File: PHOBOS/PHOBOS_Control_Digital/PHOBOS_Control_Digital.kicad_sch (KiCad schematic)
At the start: 71 parts, among them IC1 MAPS-010144-TR0500, J1 Conn_01x06, J10 PS4, J11 PWR, J2 RF_OUT, J3 USB4056-03-A_REVA2, J4 Screw_Terminal_01x02, J5 Conn_02x15_Odd_Even, J6 PS1, J7 PS2, J8 Conn_01x02, J9 PS3, SW1 KMR211GLFS, U1 SX1280IMLTRT, U2 W25Q128JVSIQ, U3 NCP1117-3.3_SOT223, U4 RP2040, Y1 C1E-52.000-10-1012-X-M, Y2 ABM8-272-T3

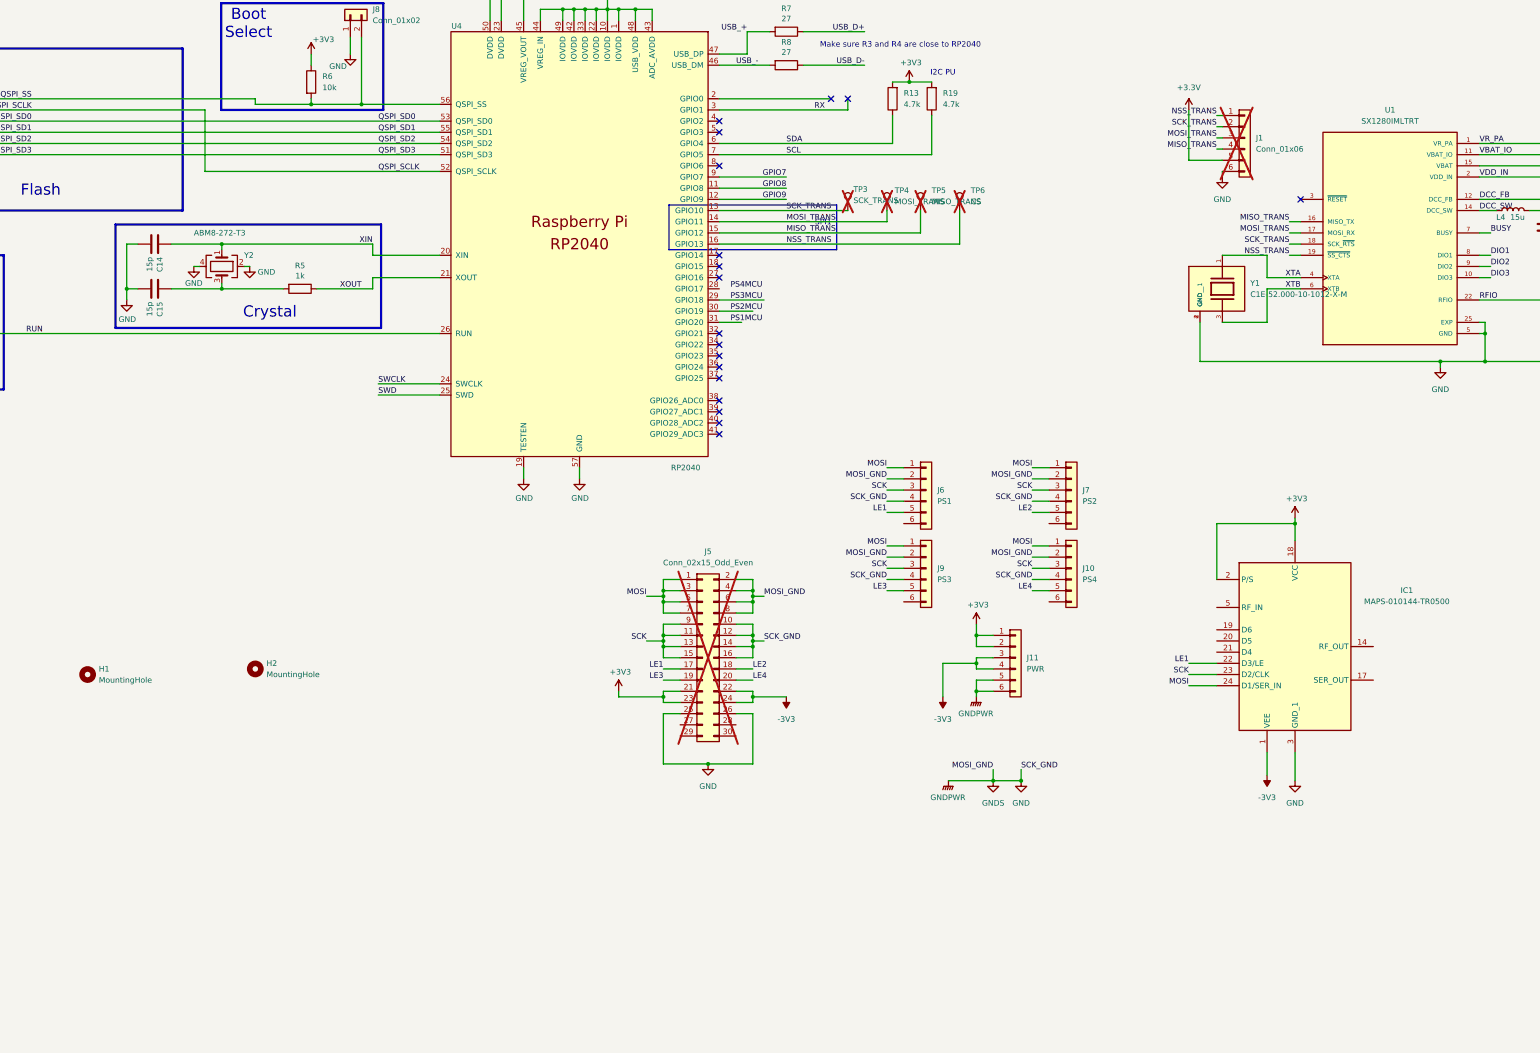
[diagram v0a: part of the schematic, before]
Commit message: connectors fine tuned (JST-GH 10 pin). 3v Inverter added. Needs routing
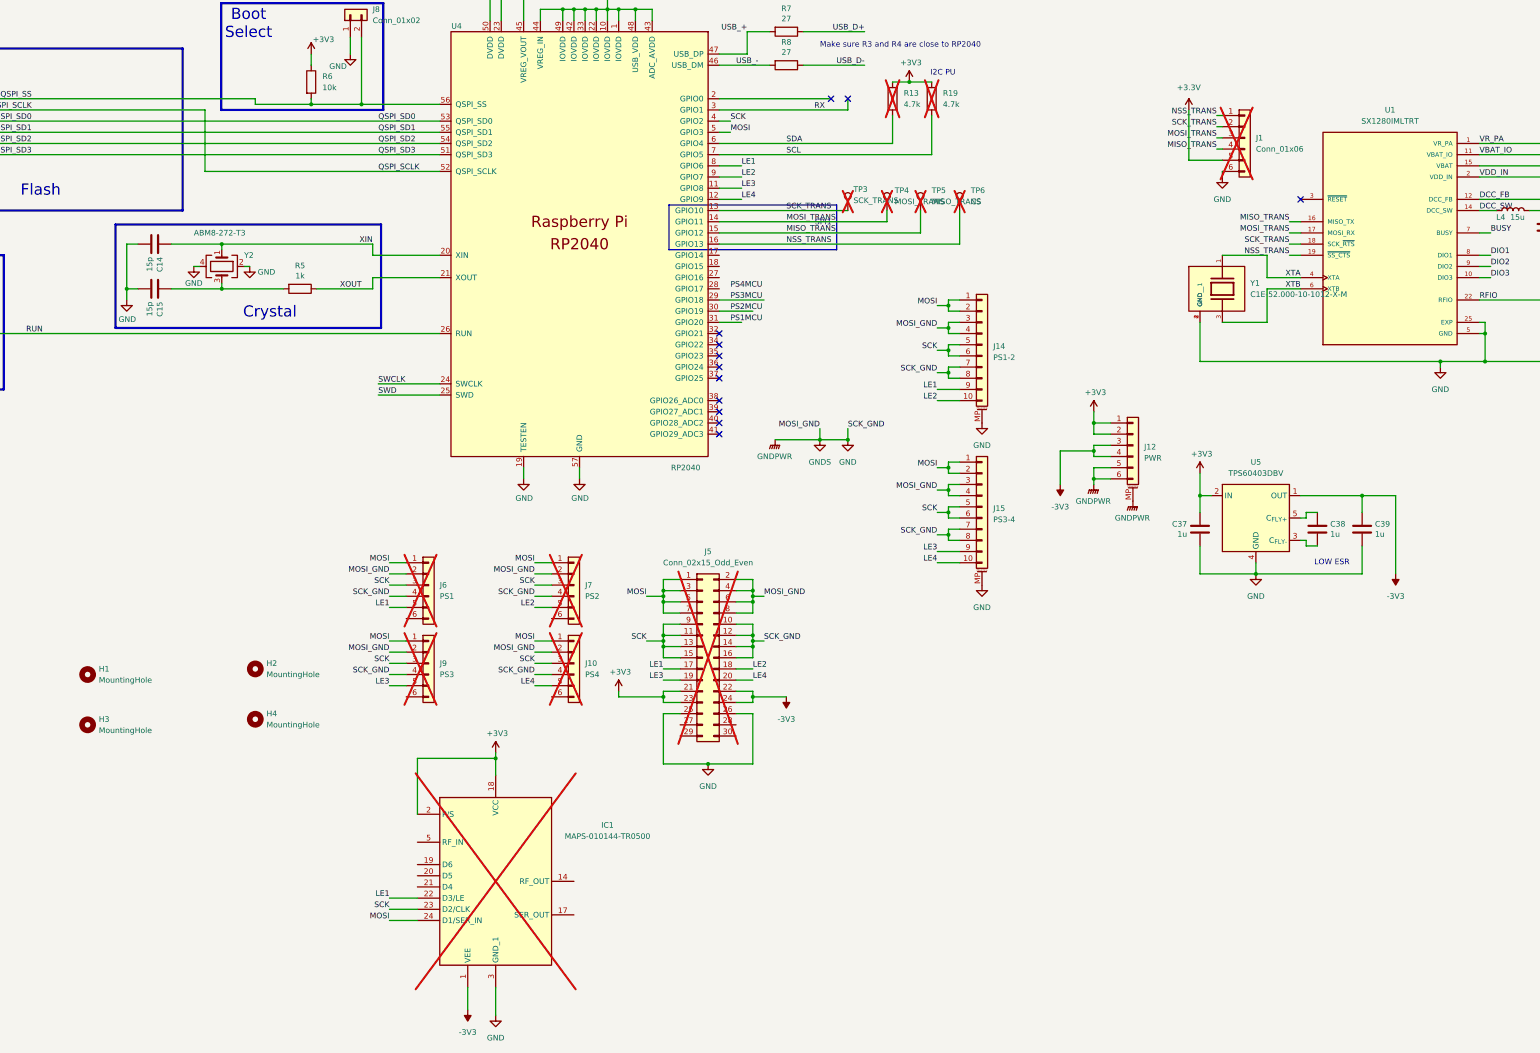
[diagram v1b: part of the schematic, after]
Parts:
- removed J11: PWR, Connector_JST:JST_GH_SM05B-GHS-TB_1x05-1MP_P1.25mm_Horizontal, symbol Connector_Generic:Conn_01x06
- added C37, C38, C39: 1u, Capacitor_SMD:C_0402_1005Metric, symbol Device:C
- added H3, H4: MountingHole, MountingHole:MountingHole_3.2mm_M3, symbol Mechanical:MountingHole
- added J12: PWR, Connector_JST:JST_GH_SM06B-GHS-TB_1x06-1MP_P1.25mm_Horizontal, symbol Connector_Generic_MountingPin:Conn_01x06_MountingPin
- added J14: PS1-2, Connector_JST:JST_GH_SM10B-GHS-TB_1x10-1MP_P1.25mm_Horizontal, symbol Connector_Generic_MountingPin:Conn_01x10_MountingPin
- added J15: PS3-4, Connector_JST:JST_GH_SM10B-GHS-TB_1x10-1MP_P1.25mm_Horizontal, symbol Connector_Generic_MountingPin:Conn_01x10_MountingPin
- added U5: TPS60403DBV, Package_TO_SOT_SMD:SOT-23-5, symbol Regulator_SwitchedCapacitor:TPS60403DBV
- IC1, J10, J6, J7, J9, R13, R19: now not fitted; now left out of the parts list
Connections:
- net GPIO7 is gone; now on net LE2: U4.9 (GPIO7)
- net GPIO8 is gone; now on net LE3: U4.11 (GPIO8)
- net GPIO9 is gone; now on net LE4: U4.12 (GPIO9)
- net +3V3: now also C37.1, J12.1 (Pin_1), J12.2 (Pin_2), U5.2 (IN)
- net -3V3: now also C39.1, J12.3 (Pin_3), J12.4 (Pin_4), U5.1 (OUT)
- net GND: now also C37.2, C39.2, J12.5 (Pin_5), J12.6 (Pin_6), J12.MP (MountPin), J14.3 (Pin_3), J14.4 (Pin_4), J14.7 (Pin_7), J14.8 (Pin_8), J14.MP (MountPin), J15.3 (Pin_3), J15.4 (Pin_4), J15.7 (Pin_7), J15.8 (Pin_8), J15.MP (MountPin), U5.4 (GND)
- net LE1: now also U4.8 (GPIO6), J14.9 (Pin_9)
- net LE2: now also J14.10 (Pin_10)
- net LE3: now also J15.9 (Pin_9)
- net LE4: now also J15.10 (Pin_10)
- net MOSI: now also U4.5 (GPIO3), J14.1 (Pin_1), J14.2 (Pin_2), J15.1 (Pin_1), J15.2 (Pin_2)
- net SCK: now also U4.4 (GPIO2), J14.5 (Pin_5), J14.6 (Pin_6), J15.5 (Pin_5), J15.6 (Pin_6)
- new net: C38.2, U5.3 (C_{FLY-})
- new net: C38.1, U5.5 (C_{FLY+})
- no-connect marks 28 -> 22
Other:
- note added: "LOW ESR"

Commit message: Centered and nicer layout.
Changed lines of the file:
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@@
 		(fields_autoplaced yes)
 		(property "Reference" "IC1"
-			(at 293.37 354.2598 0)
+			(at 270.1133 342.9 0)
 			(show_name no)
 			(do_not_autoplace no)
@@
 					(size 1.27 1.27)
 				)
+				(justify left)
 			)
 		)
 		(property "Value" "MAPS-010144-TR0500"
-			(at 293.37 356.7998 0)
+			(at 270.1133 345.44 0)
 			(show_name no)
 			(do_not_autoplace no)
@@
 					(size 1.27 1.27)
 				)
+				(justify left)
 			)
 		)

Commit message: Re-Centered. M3 bolt model added. SMA shifted to top side. Hole zones redone.
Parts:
- C37, C38, C39: footprint Capacitor_SMD:C_0402_1005Metric -> Capacitor_SMD:C_0603_1608Metric
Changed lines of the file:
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@@
 			(justify left bottom)
 		)
-		(property "Netclass" "PWR"
+		(property "Net Class" "PWR"
 			(at 183.5785 101.6 0)
 			(show_name no)
@@
 			(justify left bottom)
 		)
-		(property "Netclass" "PWR"
+		(property "Net Class" "PWR"
 			(at 165.7985 101.6 0)
 			(show_name no)
@@
 			)
 		)
-		(property "Footprint" "Capacitor_SMD:C_0402_1005Metric"
+		(property "Footprint" "Capacitor_SMD:C_0603_1608Metric"
 			(at 427.0248 290.83 0)
 			(hide yes)
@@
 			)
 		)
-		(property "Footprint" "Capacitor_SMD:C_0402_1005Metric"
+		(property "Footprint" "Capacitor_SMD:C_0603_1608Metric"
 			(at 465.7852 290.83 0)
 			(hide yes)
@@
 			)
 		)
-		(property "Footprint" "Capacitor_SMD:C_0402_1005Metric"
+		(property "Footprint" "Capacitor_SMD:C_0603_1608Metric"
 			(at 455.6252 290.83 0)
 			(hide yes)

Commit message: Images Added
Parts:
- removed IC1: MAPS-010144-TR0500, MAPS-010144-TR0500:QFN50P400X400X100-25N-D, symbol MAPS-010144-TR0500:MAPS-010144-TR0500
- removed J10: PS4, Connector_JST:JST_GH_SM05B-GHS-TB_1x05-1MP_P1.25mm_Horizontal, symbol Connector_Generic:Conn_01x06
- removed J5: Conn_02x15_Odd_Even, Package_CSP:Xilinx_CSG48_7.0x7.0mm_Layout7x7_P0.8mm, symbol Connector_Generic:Conn_02x15_Odd_Even
- removed J6: PS1, Connector_JST:JST_GH_SM05B-GHS-TB_1x05-1MP_P1.25mm_Horizontal, symbol Connector_Generic:Conn_01x06
- removed J7: PS2, Connector_JST:JST_GH_SM05B-GHS-TB_1x05-1MP_P1.25mm_Horizontal, symbol Connector_Generic:Conn_01x06
- removed J9: PS3, Connector_JST:JST_GH_SM05B-GHS-TB_1x05-1MP_P1.25mm_Horizontal, symbol Connector_Generic:Conn_01x06
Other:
- moved on the sheet: H1, H2, H3, H4

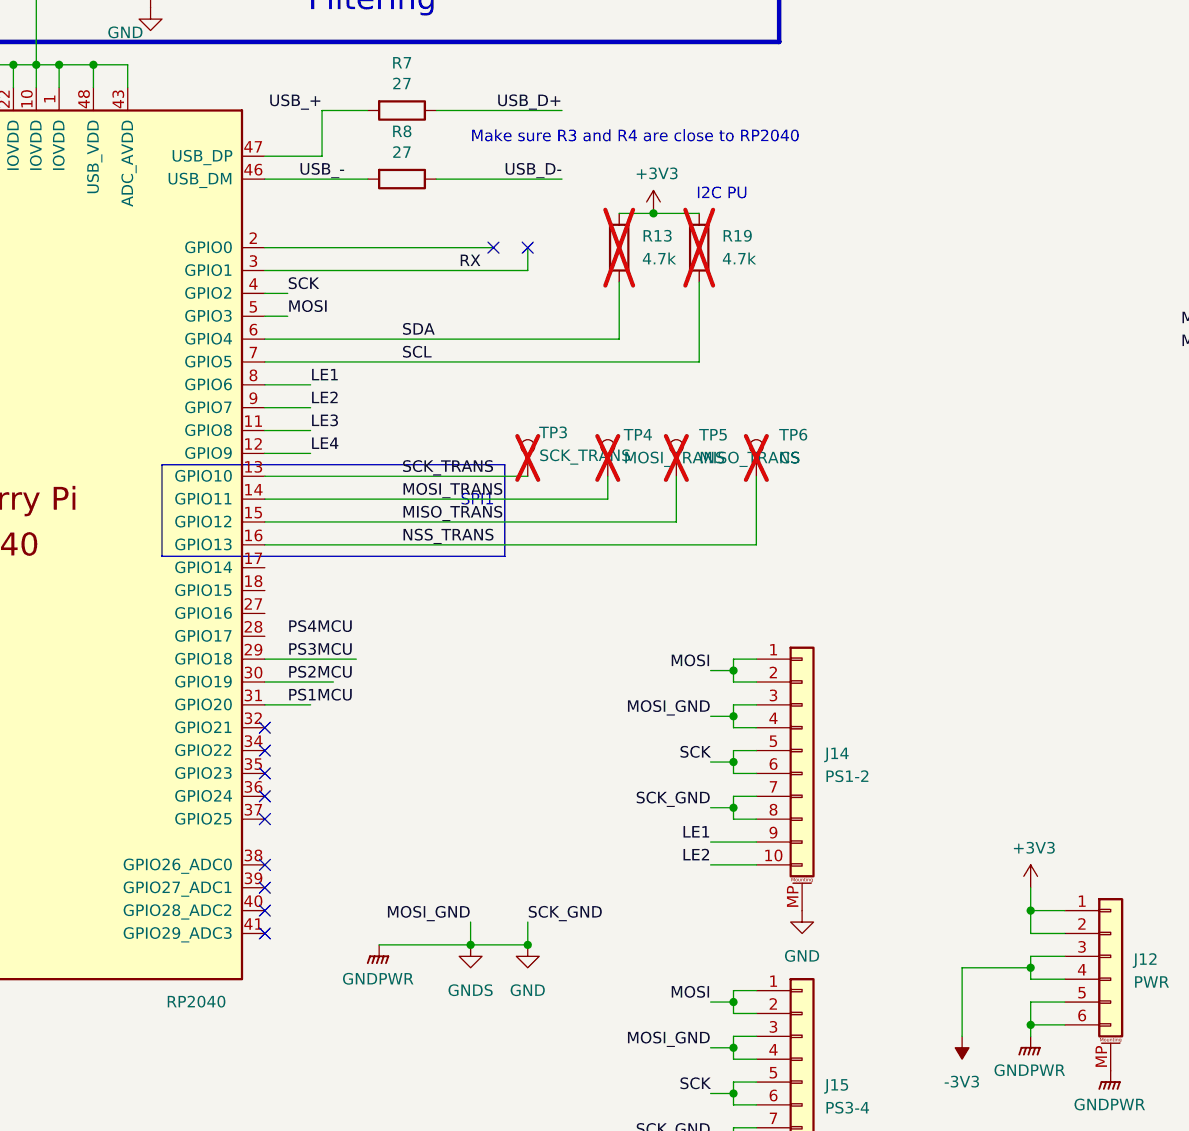
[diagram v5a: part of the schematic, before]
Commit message: uart and I2C Test Points added with a 1mm drill hole
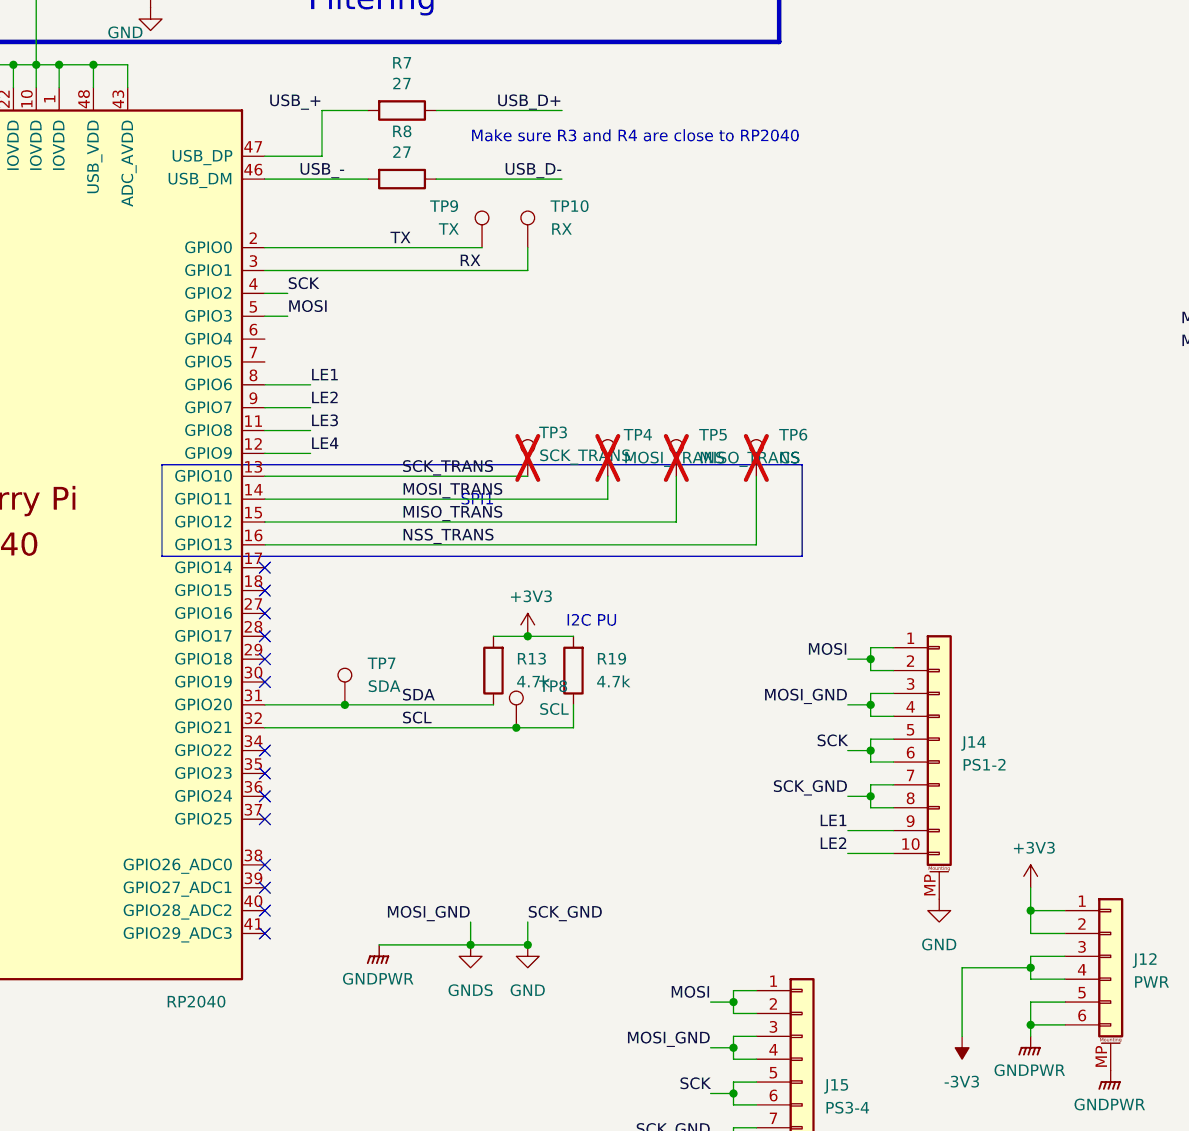
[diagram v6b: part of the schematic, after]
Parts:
- added TP10: RX, TestPoint:TestPoint_THTPad_D2.0mm_Drill1.0mm, symbol Connector:TestPoint
- added TP7: SDA, TestPoint:TestPoint_THTPad_D2.0mm_Drill1.0mm, symbol Connector:TestPoint
- added TP8: SCL, TestPoint:TestPoint_THTPad_D2.0mm_Drill1.0mm, symbol Connector:TestPoint
- added TP9: TX, TestPoint:TestPoint_THTPad_D2.0mm_Drill1.0mm, symbol Connector:TestPoint
- R13, R19: now fitted; now in the parts list
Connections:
- net PS1MCU is gone; now on net SDA: U4.31 (GPIO20)
- net RX: now also TP10.1
- net SCL: now also U4.32 (GPIO21), TP8.1; no longer U4.7 (GPIO5)
- net SDA: now also TP7.1; no longer U4.6 (GPIO4)
- net TX: now reaches U4.2 (GPIO0)
- net TX: now also TP9.1
- net PS2MCU: no longer names the net of U4.30 (GPIO19)
- net PS3MCU: no longer names the net of U4.29 (GPIO18)
- no-connect marks 22 -> 25
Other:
- moved on the sheet: J14

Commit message: i2c breakouts moved to make space for gpio22 breakout hole
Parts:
- added TP11, TP12: GPIO22, TestPoint:TestPoint_THTPad_D2.0mm_Drill1.0mm, symbol Connector:TestPoint
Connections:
- net at U4.30 (GPIO19): now also TP11.1
- net at U4.35 (GPIO23): now also TP12.1
- no-connect marks 25 -> 22
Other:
- moved on the sheet: TP7

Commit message: Updates from Overleaf
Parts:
- removed C11: 47u, Capacitor_SMD:C_0805_2012Metric_Pad1.18x1.45mm_HandSolder, symbol Device:C
- removed C12: 47u, Capacitor_SMD:C_1206_3216Metric, symbol Device:C
- removed J1: Conn_01x06, Connector_PinHeader_2.54mm:PinHeader_1x06_P2.54mm_Vertical, symbol Connector_Generic:Conn_01x06
- removed R2: 10k, Resistor_SMD:R_0402_1005Metric, symbol Device:R
- removed SW1: KMR211GLFS, External/Custom Parts:KMR2xxG_CNK, symbol KMR2xxG_CNK:KMR211GLFS
- removed TP12: GPIO22, TestPoint:TestPoint_THTPad_D2.0mm_Drill1.0mm, symbol Connector:TestPoint
- removed TP3: SCK_TRANS, TestPoint:TestPoint_Plated_Hole_D2.0mm, symbol Connector:TestPoint
- removed TP4: MOSI_TRANS, TestPoint:TestPoint_Plated_Hole_D2.0mm, symbol Connector:TestPoint
- removed TP5: MISO_TRANS, TestPoint:TestPoint_Plated_Hole_D2.0mm, symbol Connector:TestPoint
- removed TP6: CS, TestPoint:TestPoint_Plated_Hole_D2.0mm, symbol Connector:TestPoint
- added R14: 330k, Resistor_SMD:R_0402_1005Metric, symbol Device:R
- added R16: 100K, Resistor_SMD:R_0402_1005Metric, symbol Device:R
- C13, C16, C17: MFG # (none) -> CL10X106MO8NRNC
- C14, C15: MFG # (none) -> GJM1555C1H150GB01D
- C18, C19, C21, C23, C24, C25, C30, C31, C36, C7: MFG # (none) -> CL05B104KO5NNNC
- C20, C22, C37, C38, C39: MFG # (none) -> C0603X5R500-105KNP-CT
- D1, D2: MFG # (none) -> CD0603-B0340R
- D3: MFG # (none) -> QBLP601-IB5-S2897
- J12: MFG # (none) -> SM06B-GHS-TB
- J14, J15: MFG # (none) -> SM10B-GHS-TB
- J2: MFG # CONSMA001-SMD-G-T -> SMA-J-P-GF-RA-SM1
- J3: MFG # (none) -> USB4056-03-A
- J4: value Screw_Terminal_01x02 -> BATT; MFG # (none) -> OSTTE020104
- J8: value Conn_01x02 -> BOOT; now left out of the parts list
- R1, R3: MFG # (none) -> AC0402FR-7W5K1L
- R13, R19: MFG # (none) -> AC0402FR-7W4K7L
- R4: MFG # (none) -> AC0402FR-7W470RL
- R5: MFG # (none) -> AC0402FR-7W1KL
- R6: MFG # (none) -> AC0402FR-7W10KL
- R7, R8: MFG # (none) -> RC0402FR-7W27RL
- TP11: value GPIO22 -> GPIO19
- U2: MFG # (none) -> W25Q128JVSIQ
- U3: MFG # (none) -> NCP1117ST33T3G
- U4: MFG # (none) -> SC0914(13)
- U5: MFG # (none) -> TPS60403DBV
- Y2: MFG # (none) -> ABM8-272-T3
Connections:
- net +BATT: now also R14.2
- net GND: now also R16.1
- net BATT_CONT: now reaches U4.40 (GPIO28_ADC2)
- net BATT_CONT: now also R14.1, R16.2
- net RUN: no longer names the net of U4.26 (RUN)
- no-connect marks 22 -> 24
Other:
- note added: "-3V Charge Pump"
- note added: "Connectors"
- note added: "Transceiver"
- note removed: "Boot Select"
- note removed: "Exclude From Board"
- note removed: "Filtering"
- note removed: "Make sure C10 is close to pin 44 of RP2040 ***C10 is out of date. figure out***"
- note removed: "Make sure R3 and R4 are close to RP2040"
- note removed: "Reset"
- note removed: "SPI1"
- moved on the sheet: C0, C1, C10, C13, C14, C15, C16, C17, C18, C19, C2, C20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
